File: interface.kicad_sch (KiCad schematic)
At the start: 12 parts, among them J1 Conn_01x04_Pin, J2 USB_C_Receptacle_USB2.0_16P, J3 Conn_01x04_Pin, J5 Conn_01x04_Pin

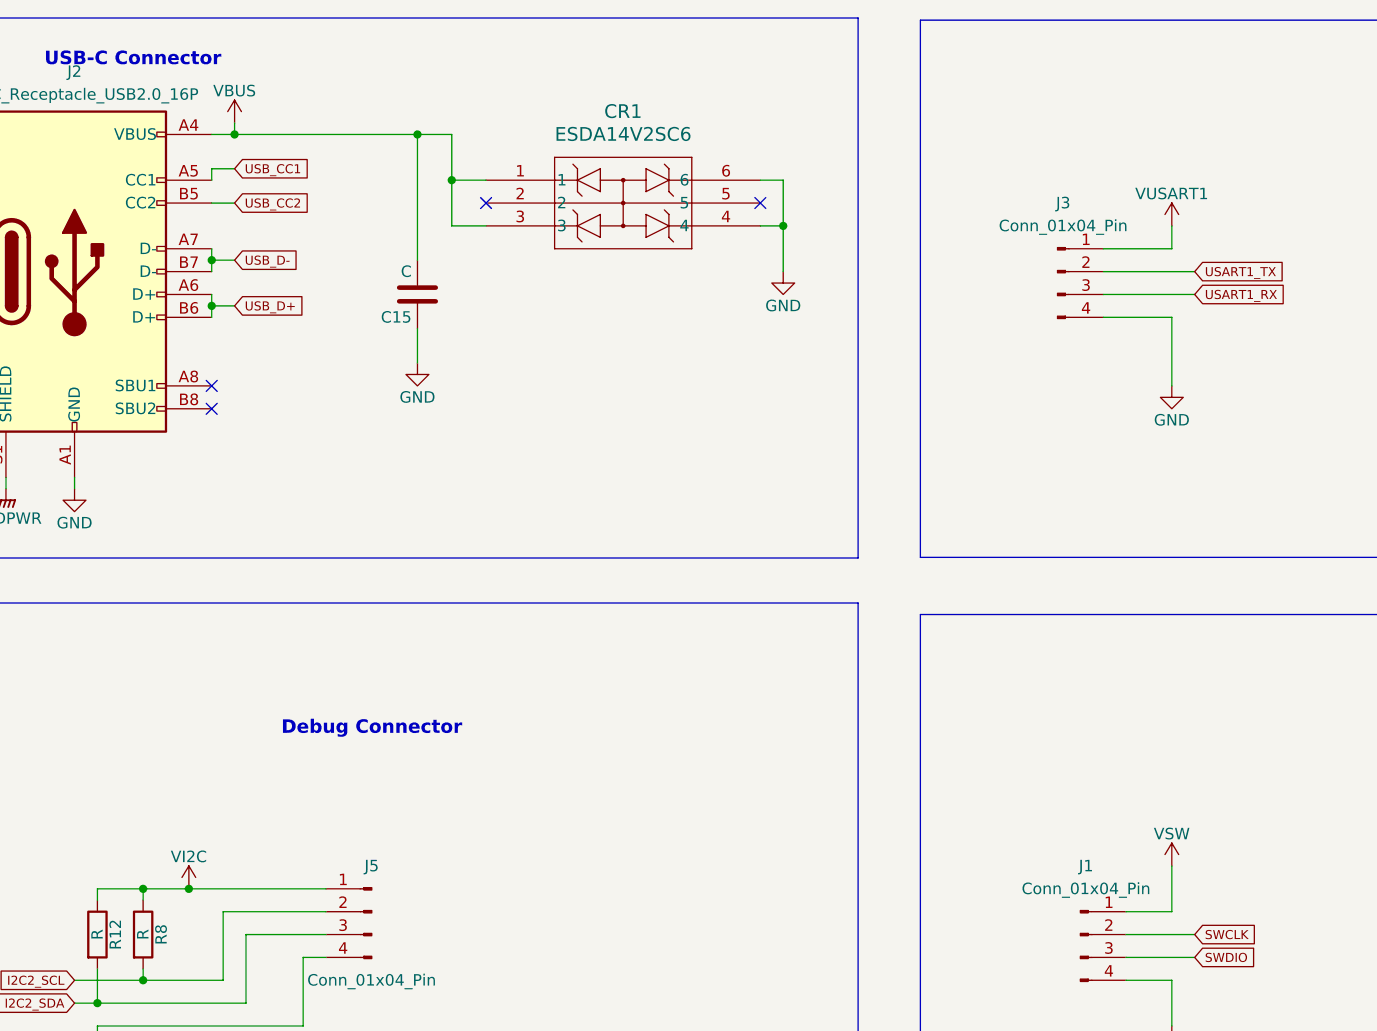
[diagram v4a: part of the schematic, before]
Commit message: isolated v sources
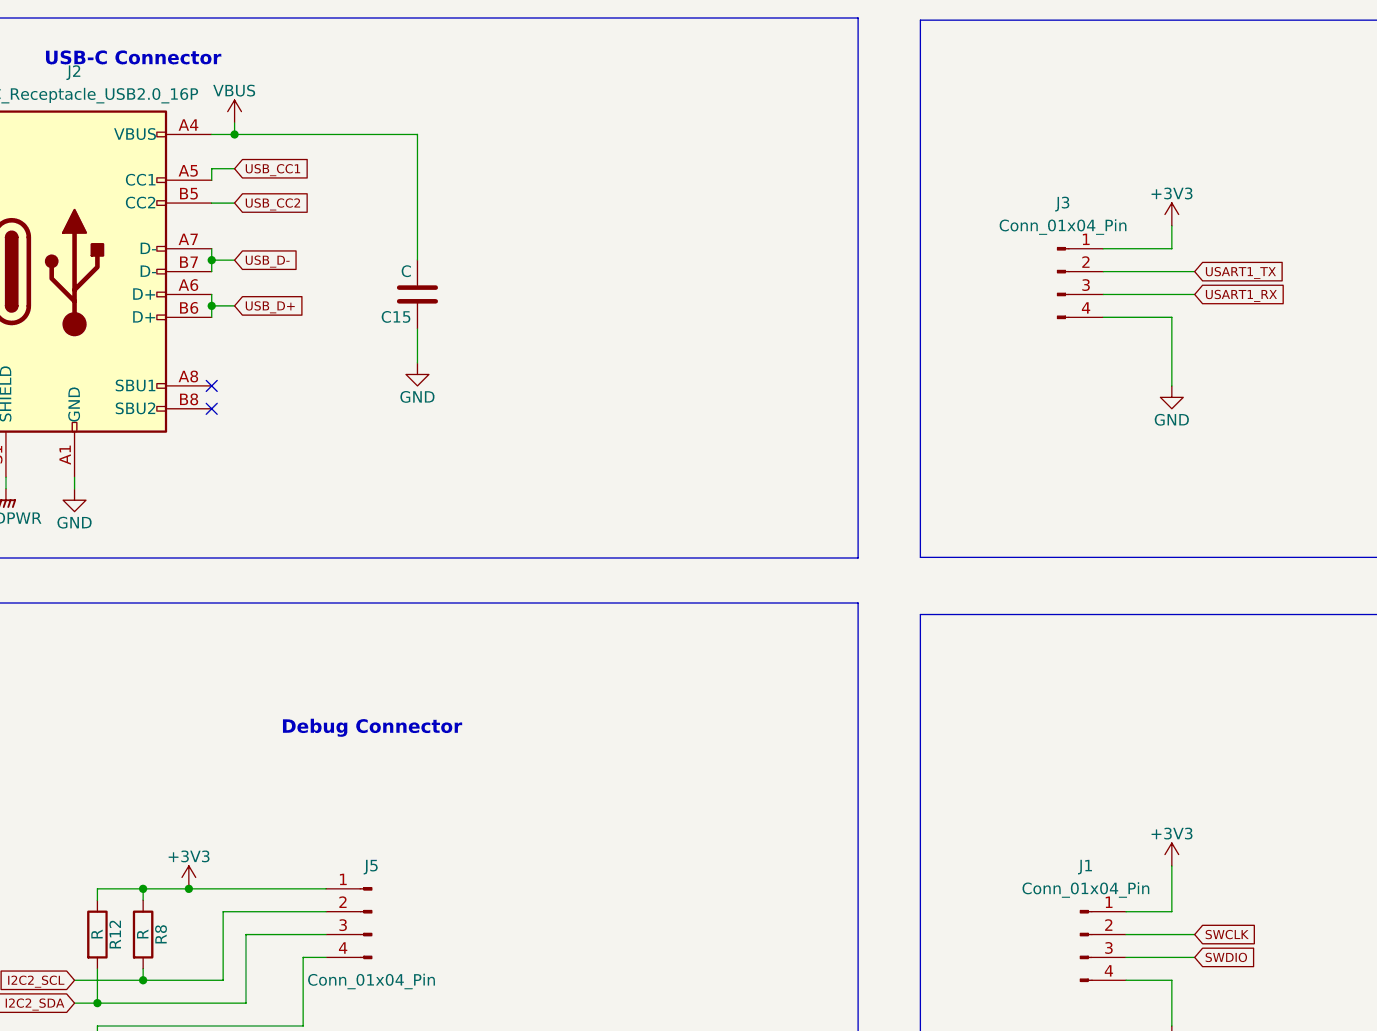
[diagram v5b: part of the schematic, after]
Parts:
- removed CR1: ESDA14V2SC6, ESDA14V2SC6:SOT23-6_1P75X3P05X0P95_STM, symbol ESDA14V2SC6:ESDA14V2SC6
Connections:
- net VSW is gone; now on net +3V3: J1.1 (Pin_1)
- net VUSART1 is gone; now on net +3V3: J3.1 (Pin_1)
- net VI2C renamed +3V3
- no-connect marks 4 -> 2

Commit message: added sheets
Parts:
- J1: footprint PPTC041LFBN_RC:PPTC041LFBN-RC -> J_1x4:PPTC041LFBN-RC
- J3, J5: footprint PPTC041LFBN_RC:SULLINS_PPTC041LFBN-RC -> J_1x4:PPTC041LFBN-RC
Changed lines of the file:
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@@
 			)
 		)
-		(property "Footprint" "PPTC041LFBN_RC:SULLINS_PPTC041LFBN-RC"
+		(property "Footprint" "J_1x4:PPTC041LFBN-RC"
 			(at 60.96 114.3 0)
 			(effects
@@
 			)
 		)
-		(property "Footprint" "PPTC041LFBN_RC:PPTC041LFBN-RC"
+		(property "Footprint" "J_1x4:PPTC041LFBN-RC"
 			(at 139.7 116.84 0)
 			(effects
@@
 			)
 		)
-		(property "Footprint" "PPTC041LFBN_RC:SULLINS_PPTC041LFBN-RC"
+		(property "Footprint" "J_1x4:PPTC041LFBN-RC"
 			(at 137.16 43.18 0)
 			(effects
